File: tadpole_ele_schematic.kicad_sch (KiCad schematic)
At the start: 8 parts, among them J1 Conn_01x03, J2 Conn_01x03, J3 Conn_01x03, J4 Conn_01x03, J5 Conn_01x03, J6 Conn_01x03, J7 Conn_01x03, J8 Conn_01x03

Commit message: added more bulkheads, and most internal electronics we could think of, not completley wired yet
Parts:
- added J10, J11: Conn_01x08, symbol Connector_Generic:Conn_01x08
- added J12: Raspberry_Pi_4, Package_DIP:DIP-24_W7.62mm, symbol Connector:Raspberry_Pi_4
- added J13: Conn_01x03, Package_SO:SOIC-20W_7.5x12.8mm_P1.27mm, symbol Connector_Generic:Conn_01x03
- added J14: Conn_01x04, symbol Connector_Generic:Conn_01x04
- added J15, J16: Conn_01x04, Package_LCC:PLCC-84_29.3x29.3mm_P1.27mm, symbol Connector_Generic:Conn_01x04
- added J17: Conn_01x02, symbol Connector_Generic:Conn_01x02
- added J9: Conn_01x06, symbol Connector_Generic:Conn_01x06
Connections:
- net GND: now also J11.5 (Pin_5), J11.6 (Pin_6), J12.14 (GND), J12.20 (GND), J12.25 (GND), J12.30 (GND), J12.34 (GND), J12.39 (GND), J12.6 (GND), J12.9 (GND), J13.1 (Pin_1), J14.4 (Pin_4), J15.1 (Pin_1), J15.2 (Pin_2), J16.1 (Pin_1), J16.2 (Pin_2)
- net +14.8V renamed +14V8
- net +14V8: now also J16.3 (Pin_3), J16.4 (Pin_4)
- new net: J12.1 (3V3), J12.17 (3V3)
- new net: J12.2 (5V), J12.4 (5V)
- new net +5V_BAR: J14.1 (Pin_1)
- new net +BATT_TO_BULK: J15.3 (Pin_3), J15.4 (Pin_4)
- new net +IDK????V: J11.7 (Pin_7), J11.8 (Pin_8)
- new net SCL_1: J12.28 (ID_SC_I2C0/GPIO01), J14.3 (Pin_3)
- new net SCL_2: J14.2 (Pin_2)
- new net SDA_1: J12.27 (ID_SD_I2C0/GPIO00)
- no-connect marks 0 -> 6
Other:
- added sheet DC-DC (DC_DC.kicad_sch)
- added sheet IMU (IMU.kicad_sch)
- added sheet Internal Camera (Internal Camera.kicad_sch)
- added sheet Killswitch Module (Killswitch Module.kicad_sch)
- added sheet Leak Sensor (Leak Sensor.kicad_sch)
- added sheet Network Switch (Network Switch.kicad_sch)
- added sheet PI Ports (Pi Ports.kicad_sch)
- sheet PWM Board: file untitled.kicad_sch -> PWM Board.kicad_sch
- note added: "? ?"
- note added: "Bar02"
- note added: "Battery Charger / Enable Thing"
- note added: "DVL"
- note added: "Dropper"
- note added: "External Camera USB"
- note added: "Start SW"
- note added: "Tether - 2 Pair ethernet + Power?????"
- note added: "This needs power of some kind"
- note added: "Wedonknowpinoutyet"
- note added: "may condense into 2 6pin hybrids, or 1 6pin and 2 3 pin"
- moved on the sheet: J1, J2, J3, J4, J5, J6, J7, J8

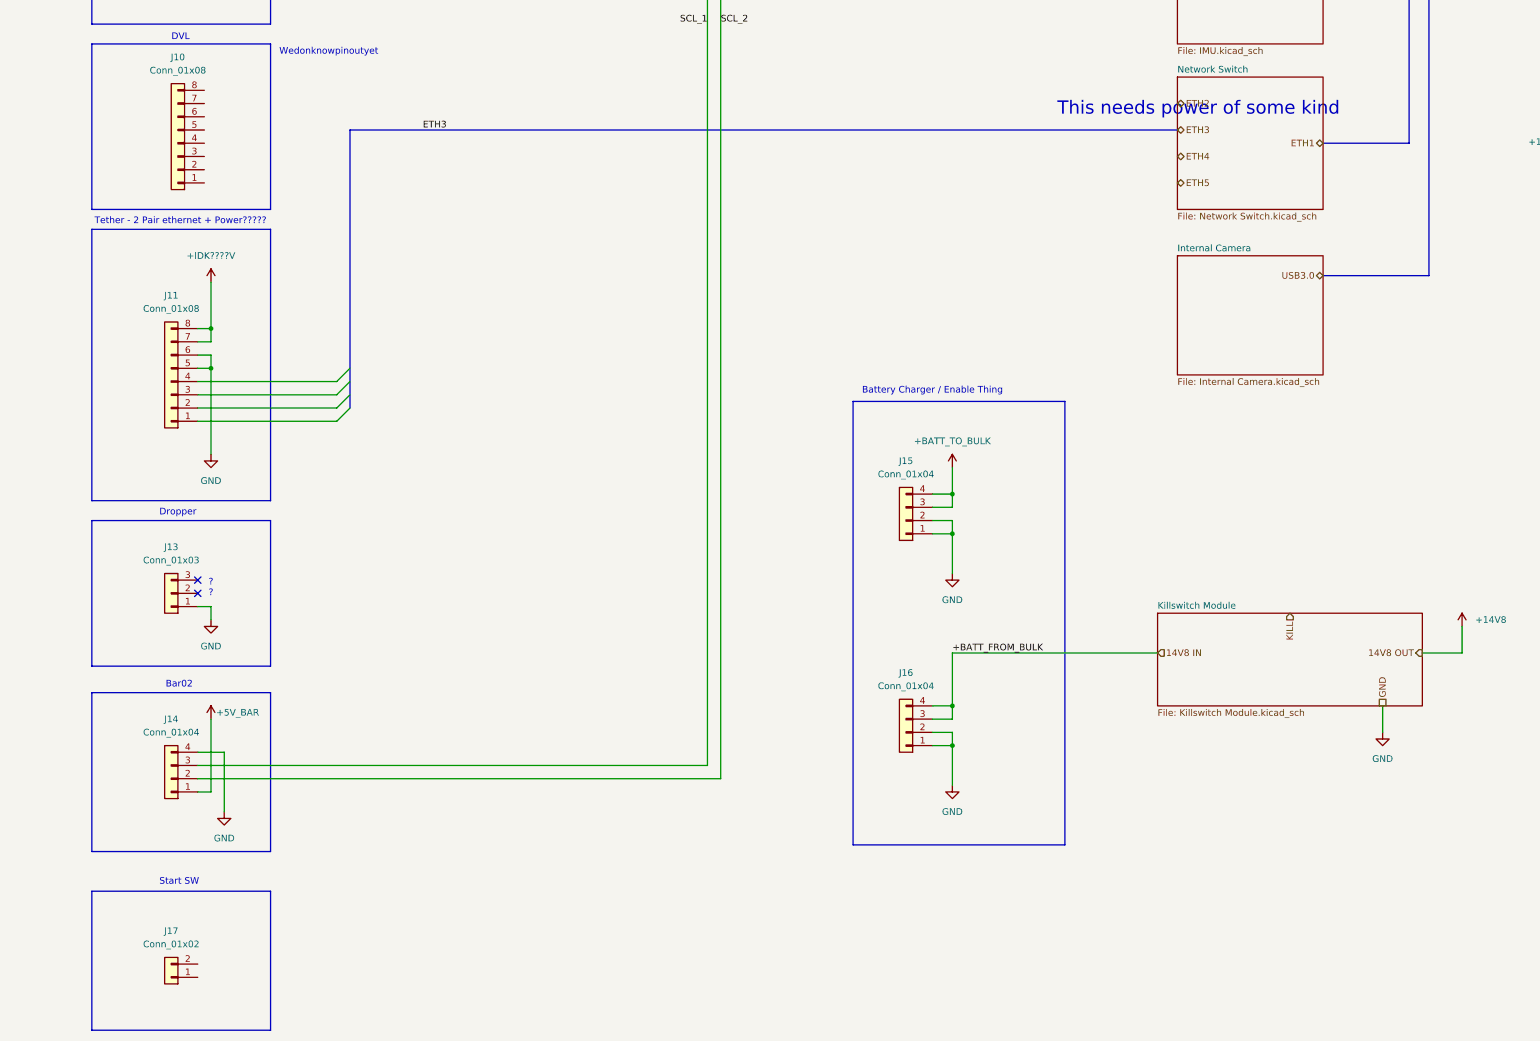
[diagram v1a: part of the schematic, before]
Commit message: changed color of some text box
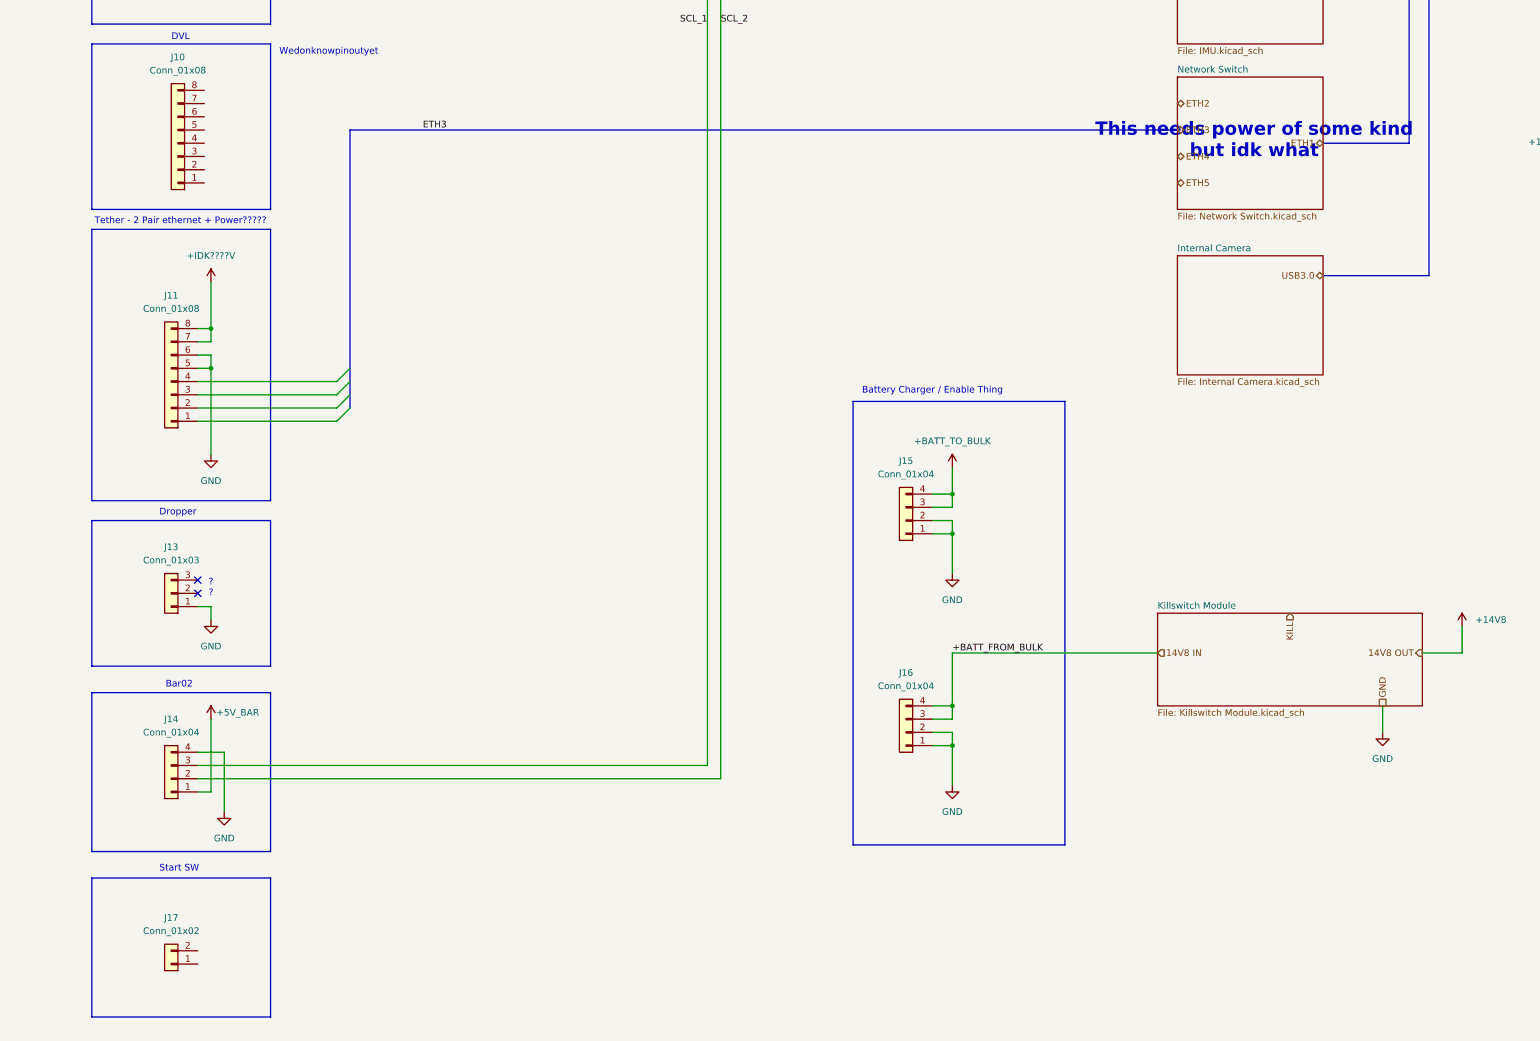
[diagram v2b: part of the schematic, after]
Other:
- note added: "This needs power of some kind but idk what"
- note removed: "This needs power of some kind"
- moved on the sheet: J17
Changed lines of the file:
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@@
 	)
 	(rectangle
-		(start 31.75 372.11)
-		(end 66.04 398.78)
+		(start 31.75 369.57)
+		(end 66.04 396.24)
 		(stroke
 			(width 0)
@@
 		)
 	)
-	(text "This needs power of some kind"
+	(text "This needs power of some kind\nbut idk what"
 		(exclude_from_sim no)
-		(at 244.094 221.996 0)
+		(at 254.762 228.092 0)
 		(effects
 			(font
 				(size 2.54 2.54)
+				(thickness 0.508)
+				(bold yes)
+				(color 255 0 7 1)
 			)
 		)
@@
 	(text "Start SW"
 		(exclude_from_sim no)
-		(at 48.514 370.332 0)
+		(at 48.514 367.792 0)
 		(effects
 			(font
@@
 	(symbol
 		(lib_id "Connector_Generic:Conn_01x02")
-		(at 46.99 388.62 180)
+		(at 46.99 386.08 180)
 		(unit 1)
 		(body_style 1)
@@
 		(fields_autoplaced yes)
 		(property "Reference" "J17"
-			(at 46.99 379.73 0)
+			(at 46.99 377.19 0)
 			(show_name no)
 			(do_not_autoplace no)
@@
 		)
 		(property "Value" "Conn_01x02"
-			(at 46.99 382.27 0)
+			(at 46.99 379.73 0)
 			(show_name no)
 			(do_not_autoplace no)
@@
 		)
 		(property "Footprint" ""
-			(at 46.99 388.62 0)
+			(at 46.99 386.08 0)
 			(hide yes)
 			(show_name no)
@@
 		)
 		(property "Datasheet" ""
-			(at 46.99 388.62 0)
+			(at 46.99 386.08 0)
 			(hide yes)
 			(show_name no)
@@
 		)
 		(property "Description" "Generic connector, single row, 01x02, script generated (kicad-library-utils/schlib/autogen/connector/)"
-			(at 46.99 388.62 0)
+			(at 46.99 386.08 0)
 			(hide yes)
 			(show_name no)

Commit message: push changes i forgot what they were
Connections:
- net +14V8 renamed +14V8_T
- net +14V8_T: no longer J16.3 (Pin_3), J16.4 (Pin_4)
- new net +14V8_G: J16.3 (Pin_3), J16.4 (Pin_4)
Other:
- added sheet PIHAT (PIHAT.kicad_sch)
- note added: "bluesub paddle"
- note removed: "This needs power of some kind but idk what"

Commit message: semifinal
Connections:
- net GND: no longer J14.4 (Pin_4)
- net +14V8_G renamed 14V8 IN
- net +5V_BAR: no longer names the net of J14.1 (Pin_1)
- net +BATT_TO_BULK renamed BATT_OUT
- net SCL_1: no longer names the net of J12.28 (ID_SC_I2C0/GPIO01)
- net SCL_1: no longer J14.3 (Pin_3)
- net SCL_2: no longer names the net of J14.2 (Pin_2)
- net SDA_1: no longer names the net of J12.27 (ID_SD_I2C0/GPIO00)
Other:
- sheet PI Ports renamed PI Board Ports
- added sheet Battery_:) (battery.kicad_sch)
- added sheet Hall effect killswitch (Hall_effect_killswitch.kicad_sch)
- note added: "5V LEAK GND"
- note added: "GND SCL SDA 5V"
- note added: "SERIAL RX SERIAL TX TX- GND VCC TX+ RX- RX+"
- moved on the sheet: J15
